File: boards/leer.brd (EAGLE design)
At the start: 34 x 48.8 mm, 55 parts, among them IC1 XMEGA128A1, IC2 7805DT, Q1 BC846BSMD, Q2 BC846BSMD, Q3 BC846BSMD, Q4 BC846BSMD, Q5 BC846BSMD, Q6 BC846BSMD, Q7 BC846BSMD, Q8 BC846BSMD

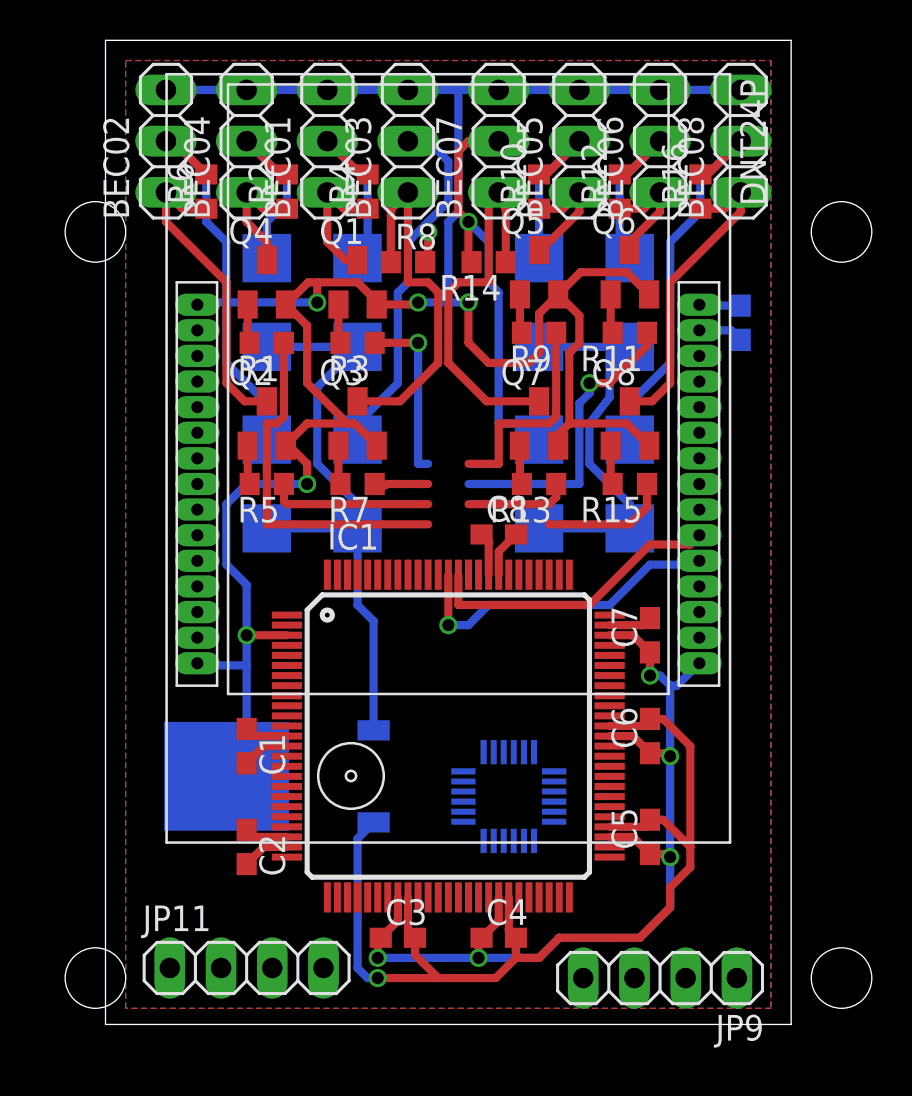
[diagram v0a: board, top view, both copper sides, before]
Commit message: modified receiver layout
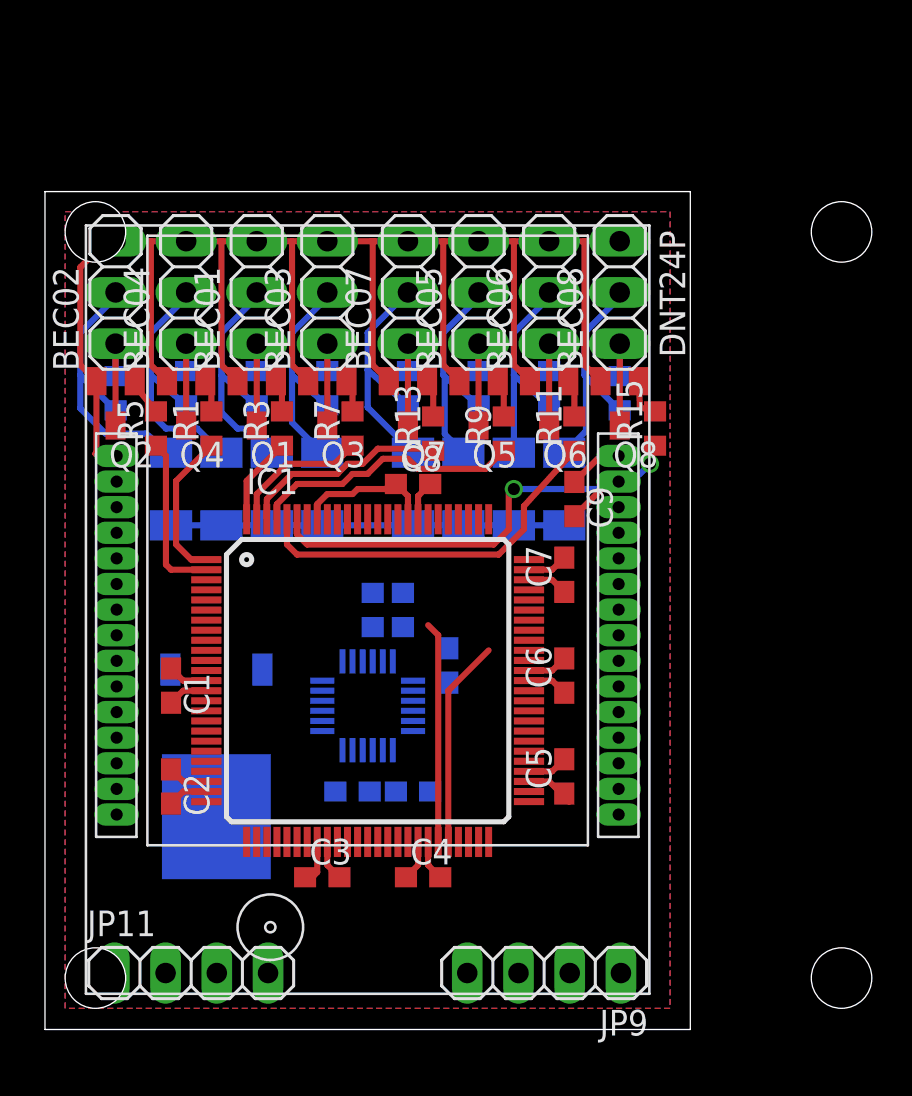
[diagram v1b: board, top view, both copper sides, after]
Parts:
- removed D8: 60V_3A, diode:SMB
- removed U$2: MPU-6050_ACC_GYRO, USER PARTS:MPU-6050_ACC_GYRO
- added C12, C13, C14: (no value), eagle-ltspice:C0603
- added D11: B 140 F, diode:SOD-123_MINI-SMA
- added R17, R20: (no value), eagle-ltspice:R0603
- added U$3: MPU-6050_ACC_GYRO, USER PARTS:MPU-6050_ACC_GYRO
- D1, D2, D3, D4, D5, D6, D7: value 60V_3A -> B 140 F; device diode:SMB -> diode:SOD-123_MINI-SMA
- moved D5 13.4 mm to (20.8, 26.8)
- moved C9 12.0 mm to (26.2, 26.2), flipped to the top
- moved D1 11.5 mm to (8.75, 26.8)
- moved R4 11.2 mm to (10.5, 31.8), flipped to the bottom, turned to 270 degrees
- moved R6 11.0 mm to (3.50, 31.5), flipped to the bottom, turned to 270 degrees
- moved R2 11.0 mm to (7.00, 31.8), flipped to the bottom, turned to 270 degrees
- moved R16 10.8 mm to (28.5, 31.5), flipped to the bottom, turned to 270 degrees
- moved D7 10.8 mm to (13.8, 26.8)
- moved R12 10.4 mm to (25.0, 31.8), flipped to the bottom, turned to 270 degrees
- moved R10 10.2 mm to (21.5, 31.8), flipped to the bottom, turned to 270 degrees
- moved D6 9.80 mm to (25.8, 26.8)
- moved BEC08 9.60 mm to (28.5, 36.5)
- moved D4 9.33 mm to (23.2, 26.8)
- moved BEC06 9.30 mm to (25.0, 36.5)
- moved BEC05 9.01 mm to (21.5, 36.5)
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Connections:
- removed net GNDS: BEC01.3, BEC02.3, BEC03.3, BEC04.3, BEC05.3, BEC06.3, BEC07.3, BEC08.3, C1.1, C2.1, C3.1, C4.1, C5.1, C6.1, C7.1, C8.1, C9.1, IC1.13, IC1.23, IC1.3, IC1.33, IC1.43, IC1.53, IC1.63, IC1.73, IC1.84, IC1.93, IC2.3, Q1.2, Q2.2, Q3.2, Q4.2, Q5.2, Q6.2, Q7.2, Q8.2, U$1.P1, U$1.P15, U$1.P16, U$1.P30
- removed net N$35: C1.2, C2.2, C3.2, C4.2, C5.2, C6.2, C7.2, C8.2, C9.2, IC1.14, IC1.24, IC1.34, IC1.44, IC1.54, IC1.64, IC1.74, IC1.83, IC2.2, U$1.P14
- new net +3V3: C1.2, C12.2, C14.2, C2.2, C3.2, C4.2, C5.2, C6.2, C7.2, C8.2, C9.2, IC1.14, IC1.24, IC1.34, IC1.44, IC1.54, IC1.64, IC1.74, IC1.83, IC2.2, R17.1, R20.1, U$1.P14, U$3.P13, U$3.P8
- new net GND: BEC01.3, BEC02.3, BEC03.3, BEC04.3, BEC05.3, BEC06.3, BEC07.3, BEC08.3, C1.1, C12.1, C13.1, C14.1, C2.1, C3.1, C4.1, C5.1, C6.1, C7.1, C8.1, C9.1, IC1.13, IC1.23, IC1.3, IC1.33, IC1.43, IC1.53, IC1.63, IC1.73, IC1.84, IC1.93, IC2.3, Q1.2, Q2.2, Q3.2, Q4.2, Q5.2, Q6.2, Q7.2, Q8.2, U$1.P1, U$1.P15, U$1.P16, U$1.P30, U$3.P1, U$3.P11, U$3.P18, U$3.P9
- new net N$37: C13.2, U$3.P10
- new net N$38: U$3.P20
- new net PF0: IC1.46, R20.2, U$3.P24
- new net PF1: IC1.45, R17.2, U$3.P23
- net N$12: now also D5.A; no longer D4.A
- net N$15: now also D1.A; no longer D5.A
- net N$17: now also D4.A; no longer D6.A
- net N$20: now also D3.A; no longer D7.A
- net N$23: now also D6.A; no longer D8.A
- net N$25: now also IC1.1; no longer IC1.95
- net N$26: now also IC1.100; no longer IC1.96
- net N$28: now also IC1.96; no longer IC1.98
- net N$29: now also IC1.2; no longer IC1.99
- net N$3: now also D11.A; no longer D1.A
- net N$30: now also IC1.98; no longer IC1.100
- net N$31: now also IC1.99; no longer IC1.1
- net N$32: now also IC1.95; no longer IC1.2
- net N$34: now also D11.C; no longer D8.C
- net N$9: now also D7.A; no longer D3.A
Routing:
- net GNDS: track 177.9 -> 0.00 mm, vias 10 -> 0
- net GND: track 0.00 -> 114.6 mm
- net N$35: track 61.8 -> 0.00 mm, vias 1 -> 0
- net N$34: track 50.4 -> 19.5 mm
- net +3V3: track 0.00 -> 18.9 mm
- net N$33: track 16.3 -> 0.00 mm, vias 1 -> 0
- net N$32: track 6.35 -> 22.1 mm, vias 0 -> 2
- net N$36: track 14.9 -> 0.00 mm
- net N$19: track 19.5 -> 5.42 mm
- net N$8: track 18.3 -> 5.42 mm
- net PF1: track 0.00 -> 11.0 mm
- net PF0: track 0.00 -> 10.3 mm
- net N$25: track 17.6 -> 7.44 mm
- net N$22: track 15.6 -> 5.67 mm
- net N$5: track 15.4 -> 5.67 mm
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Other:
- board size 34 x 48.8 mm -> 32 x 41.5 mm

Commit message: Update layout
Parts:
- added C10: (no value), eagle-ltspice:C0603
- moved IC2 14.2 mm to (21.5, 7.25), turned to 90 degrees
- moved R17 1.90 mm to (14.5, 21.5), turned to 180 degrees
- moved R20 1.27 mm to (18.0, 22.0)
- moved C12 1.25 mm to (18.2, 13.0)
- moved C13 1.25 mm to (15.2, 13.0)
- moved U$3 1.25 mm to (16.0, 17.2)
- moved D3 0.79 mm to (18.0, 27.5)
- moved D4 0.79 mm to (23.0, 27.5)
- moved D5 0.79 mm to (20.5, 27.5)
- moved D6 0.79 mm to (25.5, 27.5)
- moved C14 0.75 mm to (20.0, 18.8)
- moved D11 0.75 mm to (11.2, 27.5)
- moved D7 0.75 mm to (13.8, 27.5)
- moved D1 0.25 mm to (8.75, 27.0)
- moved D2 0.25 mm to (6.25, 27.0)
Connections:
- removed net N$38: U$3.P20
- new net N$35: C10.2, U$3.P20
- net GND: now also C10.1
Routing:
- net GND: track 114.6 -> 237.2 mm, vias 0 -> 12
- net +3V3: track 18.9 -> 129.3 mm, vias 0 -> 4
- net N$34: track 19.5 -> 48.4 mm
- net N$33: track 0.00 -> 20.5 mm, vias 0 -> 3
- net N$36: track 0.00 -> 18.3 mm, vias 0 -> 3
- net PF1: track 11.0 -> 17.9 mm, vias 0 -> 1
- net N$35: track 0.00 -> 5.11 mm
- net PF0: track 10.3 -> 15.4 mm, vias 0 -> 1
- net N$32: track 22.1 -> 25.8 mm
- net N$37: track 0.00 -> 2.76 mm
- net N$28: track 18.6 -> 20.1 mm
- net N$17: track 11.0 -> 9.69 mm
- net N$9: track 11.6 -> 10.8 mm
- net N$23: track 11.5 -> 10.9 mm
- net N$3: track 12.3 -> 11.8 mm
